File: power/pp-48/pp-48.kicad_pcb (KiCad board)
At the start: 4 copper layers, 50 x 72 mm, 110 parts, among them J101 NODE 19V, J102 FRONT PANEL, J103 AUX, J201 NODE 19V, J202 FRONT PANEL, J203 AUX, Q101 BSC070N10NS5, Q102 2N7002, Q103 2N7002, Q104 2N7002, Q105 2N7002, Q201 BSC070N10NS5, Q202 2N7002, Q203 2N7002, Q204 2N7002, Q205 2N7002, U101 LM5069MM-2, U102 INA238AIDGSR, U103 74LVC1G74, U104 ADC121C027CIMK, U105 TCA9535PWR, U106 TLP176AM, U107 TLP176AM, U108 TLP291, U201 LM5069MM-2, U202 INA238AIDGSR, U203 74LVC1G74, U204 ADC121C027CIMK, U205 TCA9535PWR, U206 TLP176AM, U207 TLP176AM, U208 TLP291

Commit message: pp-48: column 1 routed (first pass) and copied to column 2: route_hand.py (power pours, shunt vias, gate, INA238 Kelvin, In2 rotating channel and taps, +3V3 trunk, column-edge rule areas), krt-route for the rest, copycol.py; photoMOS / opto moved up on B, Q1 270, D1 / C2 by S1, INA238 270; 2 opens per column (OVK, +3V3); handoff
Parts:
- moved R119 22.5 mm to (106.0, 120.5)
- moved R219 22.5 mm to (131.0, 120.5)
- moved U106 22.5 mm to (106.0, 124.0)
- moved U107 22.5 mm to (116.0, 124.0)
- moved U206 22.5 mm to (131.0, 124.0)
- moved U207 22.5 mm to (141.0, 124.0)
- moved R121 21.5 mm to (111.0, 129.5)
- moved R122 21.5 mm to (112.5, 129.5)
- moved R221 21.5 mm to (136.0, 129.5)
- moved R222 21.5 mm to (137.5, 129.5)
- moved U108 21.5 mm to (106.0, 129.5)
- moved U208 21.5 mm to (131.0, 129.5)
- moved R120 15.2 mm to (116.0, 127.8)
- moved R220 15.2 mm to (141.0, 127.8)
- moved R127 13.3 mm to (112.6, 157.0), turned to -90 degrees
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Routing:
- net GND: track 0.00 -> 515.6 mm, vias 0 -> 66
- net +3V3: track 0.00 -> 208.9 mm, vias 0 -> 28
- net /COL2_SDA: track 0.00 -> 100.7 mm, vias 0 -> 4
- net /COL1_SDA: track 0.00 -> 75.5 mm, vias 0 -> 4
- net /Column 2/LQ: track 0.00 -> 73.7 mm, vias 0 -> 7
- net /Column 1/LQ: track 0.00 -> 73.7 mm, vias 0 -> 7
- net /COL2_SCL: track 0.00 -> 69.7 mm, vias 0 -> 7
- net /COL1_SCL: track 0.00 -> 69.7 mm, vias 0 -> 7
- net VBUS: track 0.00 -> 61.2 mm, vias 0 -> 16
- net /Column 1/RST_SW: track 0.00 -> 55.4 mm, vias 0 -> 1
- net /Column 2/RST_SW: track 0.00 -> 55.4 mm, vias 0 -> 1
- net /Column 1/PWR_SW: track 0.00 -> 52.6 mm, vias 0 -> 1
- net /Column 2/PWR_SW: track 0.00 -> 52.6 mm, vias 0 -> 1
- net /Column 2/PGD: track 0.00 -> 48.8 mm, vias 0 -> 4
- net /Column 1/PGD: track 0.00 -> 48.8 mm, vias 0 -> 4
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- added copper zone on B.Cu, net /Column 1/NODE
- added copper zone on F.Cu, net /Column 1/NODE
- added copper zone on B.Cu, net /Column 1/OUT
- added copper zone on F.Cu, net /Column 1/OUT
- added copper zone on F.Cu, net /Column 1/SENSE
- added copper zone on B.Cu, net /Column 2/NODE
- added copper zone on F.Cu, net /Column 2/NODE
- added copper zone on B.Cu, net /Column 2/OUT
- added copper zone on F.Cu, net /Column 2/OUT
- added copper zone on F.Cu, net /Column 2/SENSE
- added copper zone on In1.Cu, net GND
- added copper zone on F.Cu, net VBUS
- added copper zone on In2.Cu, net VBUS

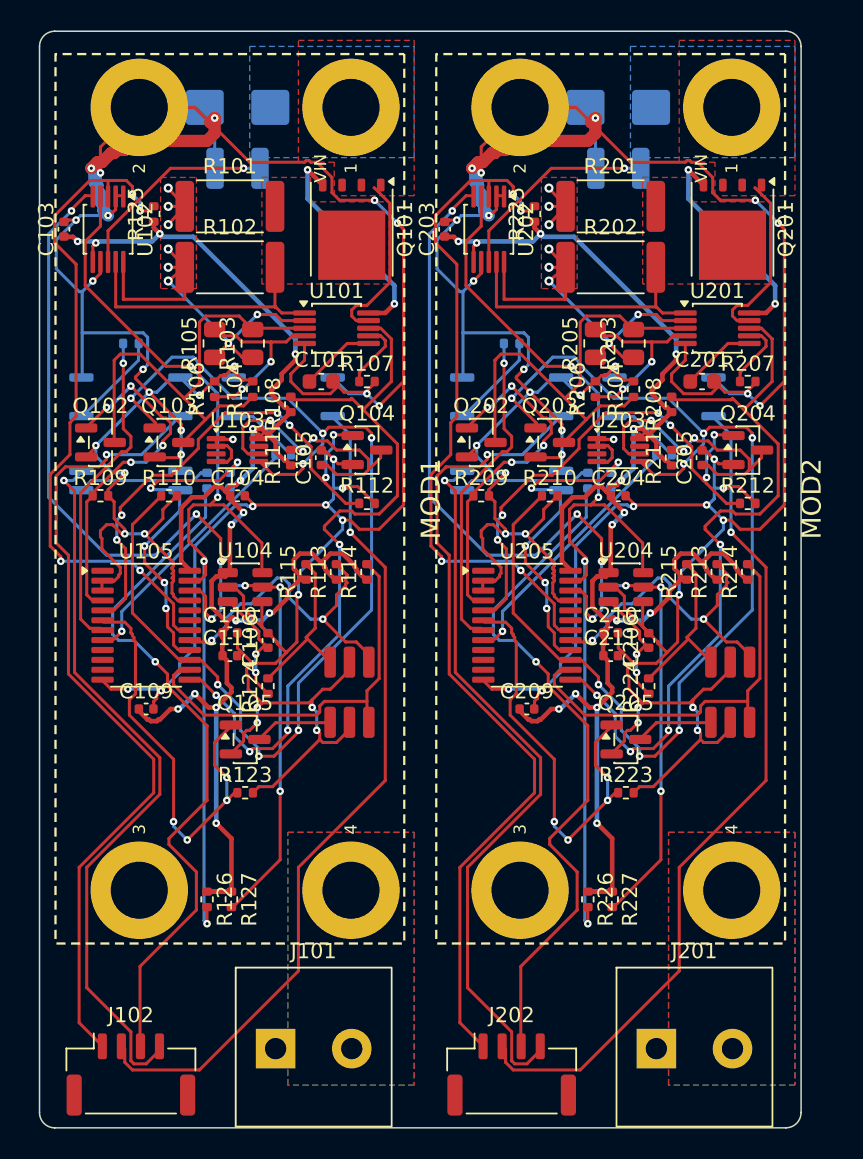
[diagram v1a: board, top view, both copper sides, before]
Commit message: pp-48: GND as F / In1 / B pours in the kept group (no GND tracks), route_hand.py re-run after KRT restores the In2 +3V3 trunk; column 1 rerouted and copied, open: OVK per column; handoff
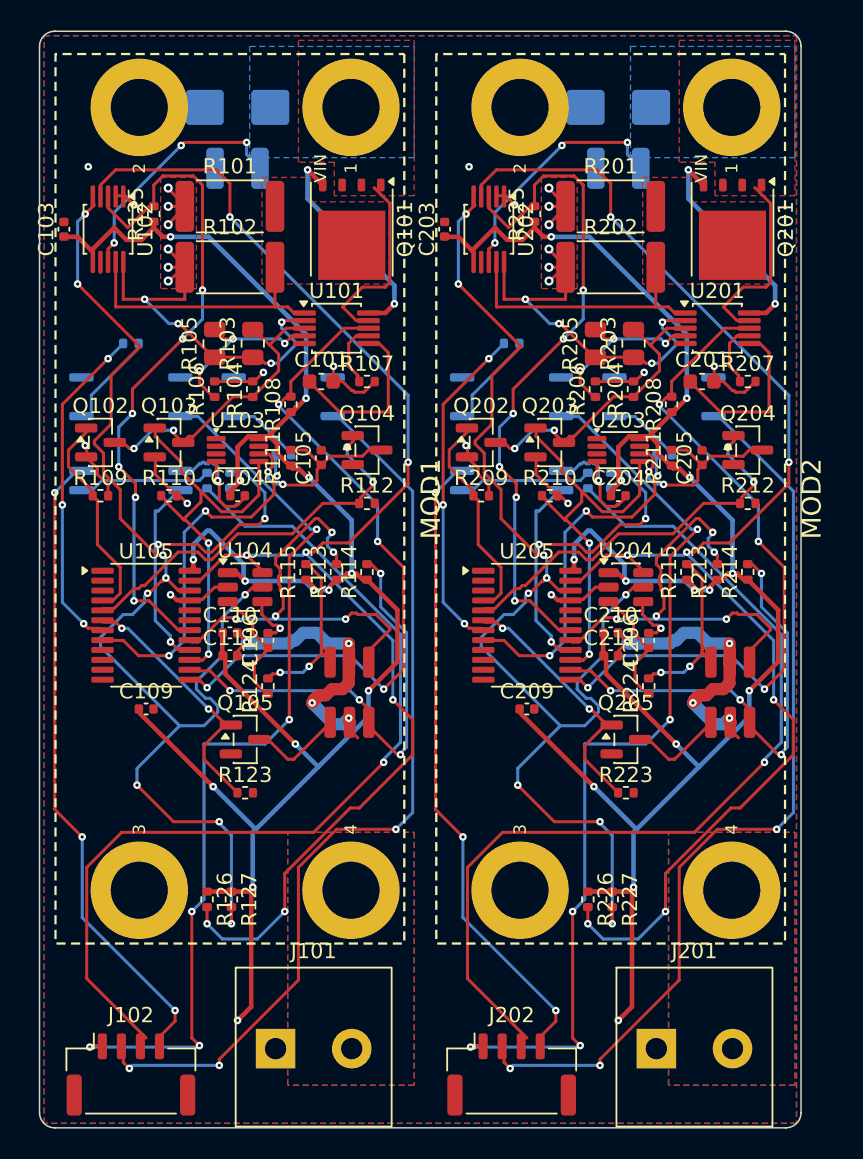
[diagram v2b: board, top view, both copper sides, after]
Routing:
- net GND: track 515.6 -> 111.9 mm, vias 66 -> 26
- net +3V3: track 208.9 -> 293.0 mm
- net /COL2_SCL: track 69.7 -> 117.6 mm, vias 7 -> 9
- net /Column 2/LQ: track 73.7 -> 27.9 mm, vias 7 -> 2
- net /Column 1/LQ: track 73.7 -> 27.9 mm, vias 7 -> 2
- net /COL2_SDA: track 100.7 -> 126.9 mm, vias 4 -> 7
- net /COL1_SDA: track 75.5 -> 101.7 mm, vias 4 -> 7
- net /COL1_SCL: track 69.7 -> 92.4 mm, vias 7 -> 9
- net /Column 1/PLED_P: track 45.5 -> 60.5 mm
- net /Column 2/PLED_P: track 45.5 -> 60.5 mm
- net /Column 2/UVLO: track 31.9 -> 19.2 mm, vias 0 -> 2
- net /Column 1/UVLO: track 31.9 -> 19.2 mm, vias 0 -> 2
- net /Column 2/RUNOFF: track 27.8 -> 16.8 mm, vias 4 -> 2
- net /Column 1/RUNOFF: track 27.8 -> 16.8 mm, vias 4 -> 2
- net /Column 1/LCLR: track 34.6 -> 25.1 mm, vias 6 -> 2
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- added copper zone on B.Cu, net GND
- added copper zone on F.Cu, net GND

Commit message: pp-48: placement rework by signal flow (expander in the middle, pins reassigned by board side; enable chain and latch under the LM5069; ID ADC, RUN FET, pull-ups around the socket; photoMOS / opto back lower left on B); column 1 rerouted and copied, 0 unconnected; gndstitch.py ties floating GND pour islands to In1; handoff
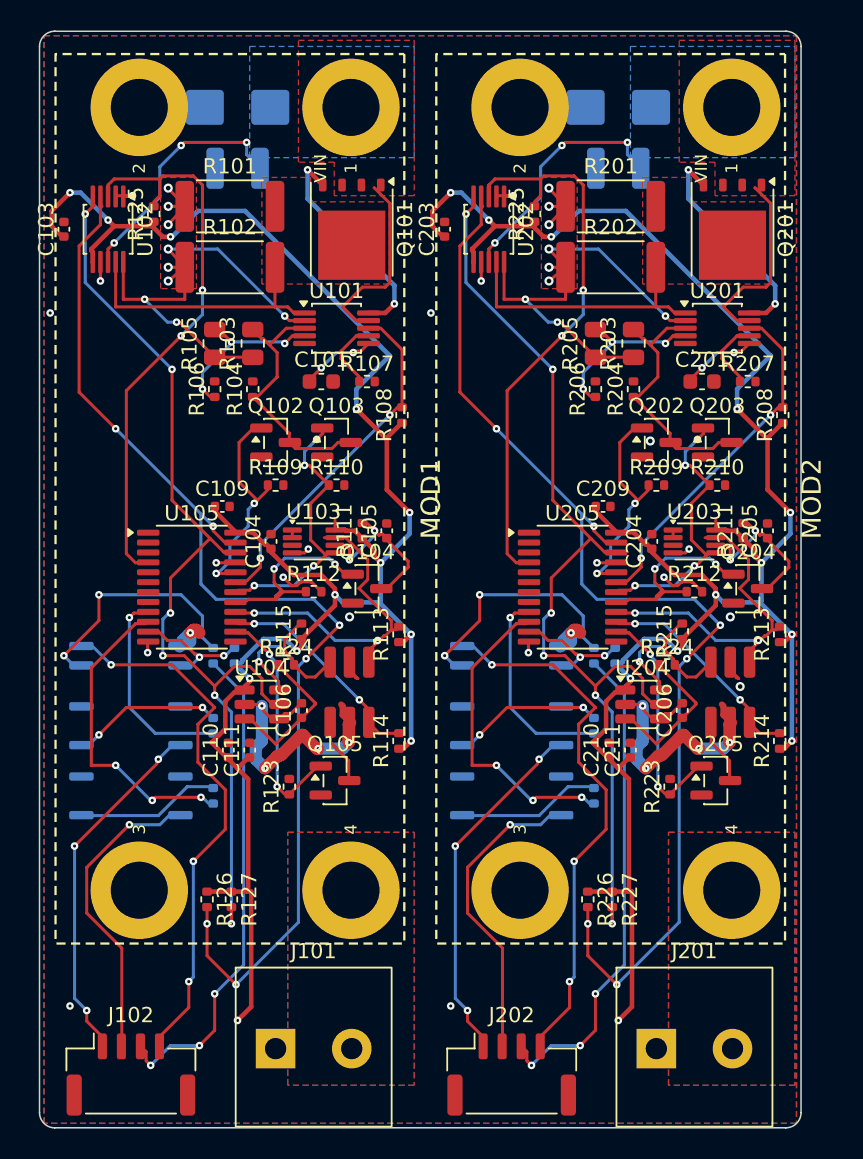
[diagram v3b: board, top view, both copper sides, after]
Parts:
- moved U107 28.0 mm to (106.0, 150.2)
- moved U207 28.0 mm to (131.0, 150.2)
- moved R119 25.7 mm to (111.4, 145.6), turned to 90 degrees
- moved R219 25.7 mm to (136.4, 145.6), turned to 90 degrees
- moved R120 22.9 mm to (111.4, 150.2), turned to 90 degrees
- moved R220 22.9 mm to (136.4, 150.2), turned to 90 degrees
- moved U106 21.6 mm to (106.0, 145.6)
- moved U206 21.6 mm to (131.0, 145.6)
- moved C109 14.2 mm to (112.0, 131.2)
- moved C209 14.2 mm to (137.0, 131.2)
- moved R109 11.5 mm to (115.5, 129.8)
- moved R209 11.5 mm to (140.5, 129.8)
- moved R121 11.5 mm to (111.4, 141.0)
- moved R221 11.5 mm to (136.4, 141.0)
- moved R122 11.5 mm to (112.8, 141.0)
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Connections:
- U105 pad 10: unconnected-(U105-P06-Pad10) -> /Column 1/RSTD
- U105 pad 11: unconnected-(U105-P07-Pad11) -> /Column 1/LED
- U105 pad 13: /Column 1/PGD -> unconnected-(U105-P10-Pad13)
- U105 pad 14: /Column 1/PG -> /Column 1/RUNOFF
- U105 pad 15: /Column 1/LQ -> /Column 1/PG
- U105 pad 16: /Column 1/LED -> /Column 1/OVK
- U105 pad 17: /Column 1/OVK -> /Column 1/LCLR
- U105 pad 18: /Column 1/INA_AL -> /Column 1/LQ
- U105 pad 19: unconnected-(U105-P16-Pad19) -> /Column 1/PGD
- U105 pad 20: unconnected-(U105-P17-Pad20) -> /Column 1/OFF
- U105 pad 4: /Column 1/OFF -> /Column 1/INA_AL
- U105 pad 5: /Column 1/LCLR -> unconnected-(U105-P01-Pad5)
- U105 pad 6: /Column 1/RUNOFF -> unconnected-(U105-P02-Pad6)
- U105 pad 7: /Column 1/PWRD -> unconnected-(U105-P03-Pad7)
- U105 pad 8: /Column 1/RSTD -> unconnected-(U105-P04-Pad8)
- U105 pad 9: unconnected-(U105-P05-Pad9) -> /Column 1/PWRD
- U205 pad 10: unconnected-(U205-P06-Pad10) -> /Column 2/RSTD
- U205 pad 11: unconnected-(U205-P07-Pad11) -> /Column 2/LED
- U205 pad 13: /Column 2/PGD -> unconnected-(U205-P10-Pad13)
- U205 pad 14: /Column 2/PG -> /Column 2/RUNOFF
- U205 pad 15: /Column 2/LQ -> /Column 2/PG
- U205 pad 16: /Column 2/LED -> /Column 2/OVK
- U205 pad 17: /Column 2/OVK -> /Column 2/LCLR
- U205 pad 18: /Column 2/INA_AL -> /Column 2/LQ
- U205 pad 19: unconnected-(U205-P16-Pad19) -> /Column 2/PGD
- U205 pad 20: unconnected-(U205-P17-Pad20) -> /Column 2/OFF
- U205 pad 4: /Column 2/OFF -> /Column 2/INA_AL
- U205 pad 5: /Column 2/LCLR -> unconnected-(U205-P01-Pad5)
- U205 pad 6: /Column 2/RUNOFF -> unconnected-(U205-P02-Pad6)
- U205 pad 7: /Column 2/PWRD -> unconnected-(U205-P03-Pad7)
- U205 pad 8: /Column 2/RSTD -> unconnected-(U205-P04-Pad8)
- U205 pad 9: unconnected-(U205-P05-Pad9) -> /Column 2/PWRD
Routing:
- net GND: track 111.9 -> 67.7 mm, vias 26 -> 30
- net /Column 2/RST_SW: track 59.7 -> 19.5 mm, vias 3 -> 1
- net /Column 1/RST_SW: track 59.7 -> 19.5 mm, vias 3 -> 1
- net /Column 2/PWR_SW: track 59.7 -> 22.7 mm, vias 5 -> 3
- net /Column 1/PWR_SW: track 59.7 -> 22.7 mm, vias 5 -> 3
- net /Column 1/PLED_P: track 60.5 -> 32.4 mm, vias 1 -> 3
- net /Column 2/PLED_P: track 60.5 -> 32.4 mm, vias 1 -> 3
- net /Column 2/PGD: track 44.9 -> 22.1 mm, vias 4 -> 2
- net /Column 1/PGD: track 44.9 -> 22.1 mm, vias 4 -> 2
- net /Column 1/LED: track 25.3 -> 6.32 mm, vias 3 -> 2
- net /Column 2/LED: track 25.3 -> 6.32 mm, vias 3 -> 2
- net /Column 2/PG: track 28.2 -> 13.2 mm, vias 4 -> 2
- net /Column 1/PG: track 28.2 -> 13.2 mm, vias 4 -> 2
- net /COL1_SCL: track 92.4 -> 77.5 mm, vias 9 -> 6
- net /COL2_SCL: track 117.6 -> 102.8 mm, vias 9 -> 6
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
